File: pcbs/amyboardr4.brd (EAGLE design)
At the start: 111.2 x 50 mm, 123 parts, among them J1 52601-G10-8LF, M13 M2.5, M14 M2.5, M15 M2.5, M16 M2.5, Q2 S8050, Q5 S8050, U1 PCM9211PT, U13 HX3608, U15 H11L1SR2M, U16 SPX3819, U2 ESP32­S2­SOLO, Y1 ABM10W-22.5792MHZ-8-K1Z-T3

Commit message: moving around
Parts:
- Y1: value ABM10W-22.5792MHZ-8-K1Z-T3 -> 22.5792MHZ
- moved L4 101.9 mm to (6.10, 9.14)
- moved C85 79.4 mm to (100.8, 22.6), turned to 90 degrees
- moved SD1 78.8 mm to (91.4, 36.6), turned to 90 degrees
- moved U2 77.6 mm to (13.0, 23.1), turned to 90 degrees
- moved R72 77.4 mm to (94.5, 33.3)
- moved R102 77.4 mm to (100.8, 19.3), turned to 0 degrees
- moved C106 77.2 mm to (95.5, 31.0)
- moved C108 75.0 mm to (100.3, 31.0), turned to 90 degrees
- moved U16 74.8 mm to (100.3, 26.9)
- moved C109 72.8 mm to (89.2, 32.3)
- moved C18 65.8 mm to (4.06, 38.6), turned to 90 degrees
- moved C110 64.3 mm to (86.1, 32.8)
- moved HOST 61.8 mm to (67.1, 36.3), turned to 180 degrees
- moved R88 61.4 mm to (82.3, 32.8), turned to 90 degrees
- moved C88 48.0 mm to (29.0, 14.7)
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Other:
- board size 111.2 x 50 mm -> 107.9 x 50 mm

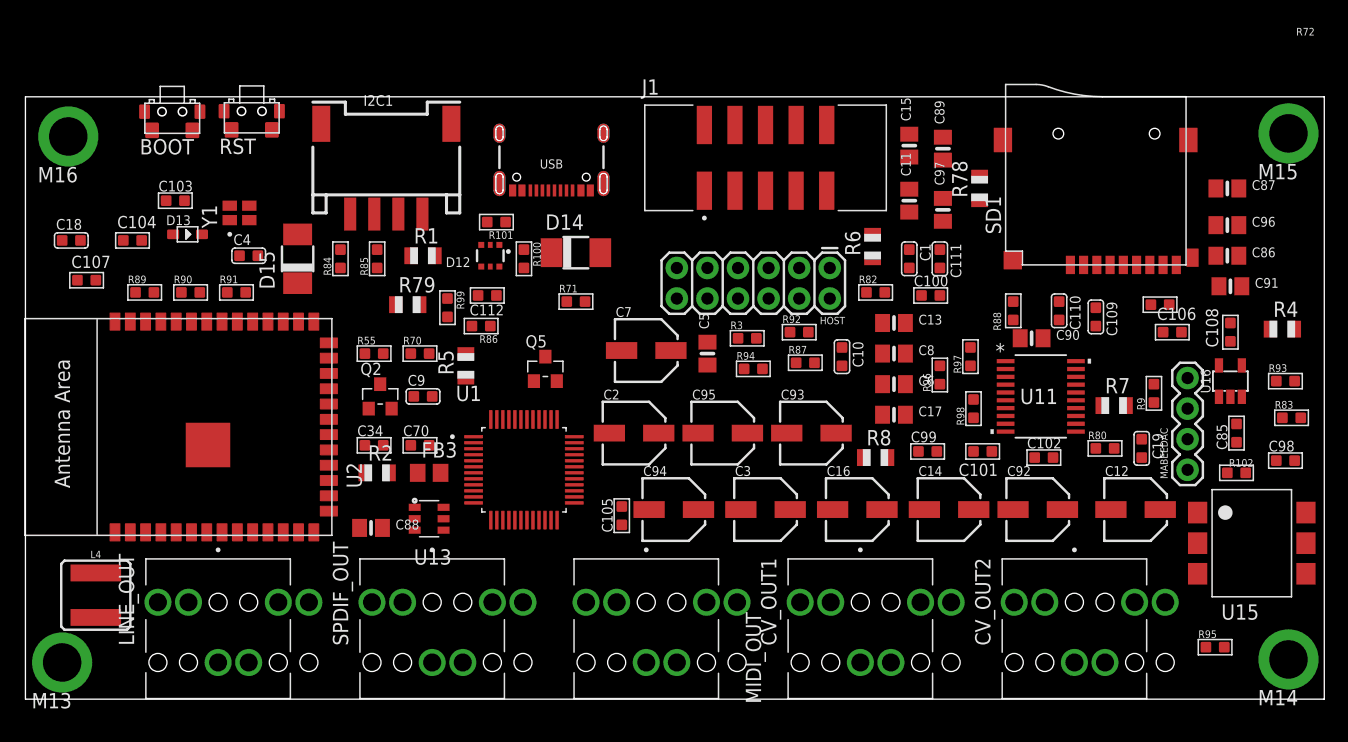
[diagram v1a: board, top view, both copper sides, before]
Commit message: r4 with top jacks
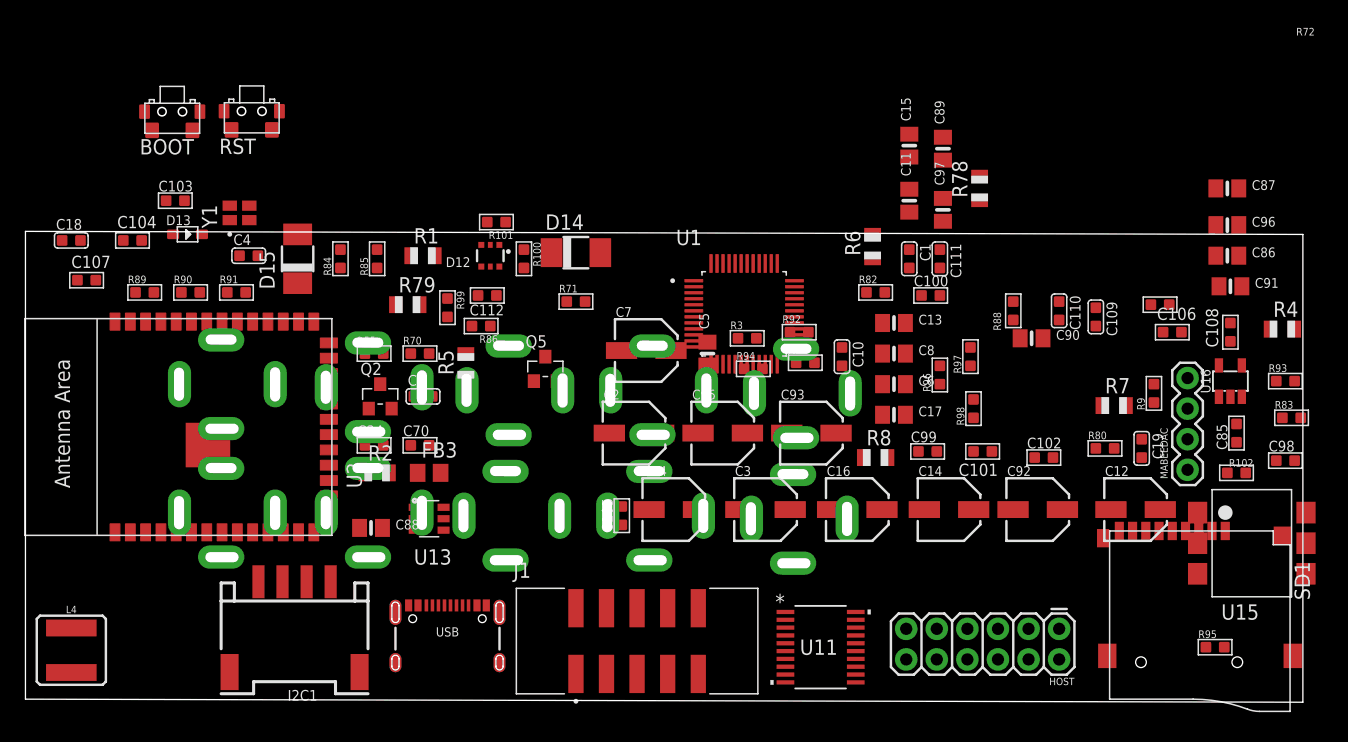
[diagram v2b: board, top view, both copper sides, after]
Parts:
- removed M13, M14, M15, M16: M2.5, sale:M2.5
- removed SPDIF_OUT: SJ1-3543, SJ1-3543:CUI_SJ1-3543
- added U$16: NV-PJ3410_STEREO, PJ3410_sockets:NV-PJ3410_SOCKET
- CV_IN1, CV_IN2, CV_OUT1, CV_OUT2, LINE_IN, LINE_OUT, MIDI_IN, MIDI_OUT, SPDIF_IN: value SJ1-3543 -> NV-PJ3410_STEREO; device SJ1-3543:CUI_SJ1-3543 -> PJ3410_sockets:NV-PJ3410_SOCKET
- moved J1 41.5 mm to (51.1, 5.33)
- moved HOST 35.5 mm to (86.1, 6.35)
- moved USB 34.9 mm to (35.3, 8.64), turned to 0 degrees
- moved CV_IN2 34.0 mm to (64.3, 25.9), turned to 270 degrees
- moved I2C1 31.7 mm to (22.6, 10.2), turned to 180 degrees
- moved CV_IN1 30.1 mm to (52.3, 26.2), turned to 270 degrees
- moved PCM5101 27.7 mm to (66.3, 4.83)
- moved MIDI_IN 26.6 mm to (40.4, 26.2), turned to 270 degrees
- moved CV_OUT2 26.2 mm to (64.0, 15.5), flipped to the bottom, turned to 270 degrees
- moved SPDIF_IN 24.2 mm to (28.7, 26.4), turned to 270 degrees
- moved LINE_IN 23.2 mm to (16.5, 26.7), turned to 270 degrees
- moved SD1 22.5 mm to (95.5, 14.5), turned to 270 degrees
- moved U1 22.4 mm to (59.9, 32.5)
- moved CV_OUT1 21.3 mm to (52.1, 15.7), flipped to the bottom, turned to 270 degrees
- moved MIDI_OUT 16.9 mm to (40.1, 15.7), flipped to the bottom, turned to 270 degrees
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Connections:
- removed net N$15: CV_OUT2.1
- net AGND: now also LINE_IN.GND, LINE_OUT.GND; no longer LINE_IN.1, LINE_OUT.1
- net GND: now also CV_IN1.GND, CV_OUT1.GND, CV_OUT2.GND, MIDI_IN.GND, MIDI_OUT.GND, SPDIF_IN.GND, U$16.GND; no longer CV_IN1.1, CV_IN2.1, CV_OUT1.1, M13.1, M14.1, M15.1, M16.1, MIDI_IN.1, MIDI_OUT.1, SPDIF_IN.1, SPDIF_OUT.1
- net LIN: now also LINE_IN.LEFT/TIP; no longer LINE_IN.2
- net LOUT: now also LINE_OUT.LEFT/TIP; no longer LINE_OUT.2
- net MABEEDAC_VOUT0: now also CV_OUT1.LEFT/TIP; no longer CV_OUT1.2
- net MABEEDAC_VOUT1: now also CV_OUT2.LEFT/TIP; no longer CV_OUT2.2
- net N$10: now also SPDIF_IN.RIGHT/RING; no longer SPDIF_IN.3
- net N$11: now also CV_OUT1.RIGHT/RING; no longer CV_OUT1.3
- net N$12: now also CV_OUT2.RIGHT/RING; no longer CV_OUT2.3
- net N$13: now also CV_IN1.RIGHT/RING; no longer CV_IN1.3
- net N$14: now also CV_IN2.RIGHT/RING; no longer CV_IN2.3
- net N$17: now also CV_IN1.LEFT/TIP; no longer CV_IN1.2
- net N$19: now also CV_IN2.LEFT/TIP; no longer CV_IN2.2
- net N$55: now also MIDI_IN.LEFT/TIP; no longer MIDI_IN.2
- net N$56: now also MIDI_IN.RIGHT/RING; no longer MIDI_IN.3
- net N$58: now also MIDI_OUT.LEFT/TIP; no longer MIDI_OUT.2
- net N$59: now also MIDI_OUT.RIGHT/RING; no longer MIDI_OUT.3
- net N$9: now also U$16.RIGHT/RING; no longer SPDIF_OUT.3
- net RIN: now also LINE_IN.RIGHT/RING; no longer LINE_IN.3
- net ROUT: now also LINE_OUT.RIGHT/RING; no longer LINE_OUT.3
- net SPDIFIN_SIGNAL: now also SPDIF_IN.LEFT/TIP; no longer SPDIF_IN.2
- net SPDIFOUT_SIGNAL: now also U$16.LEFT/TIP; no longer SPDIF_OUT.2
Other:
- board size 107.9 x 50 mm -> 106.1 x 39.1 mm

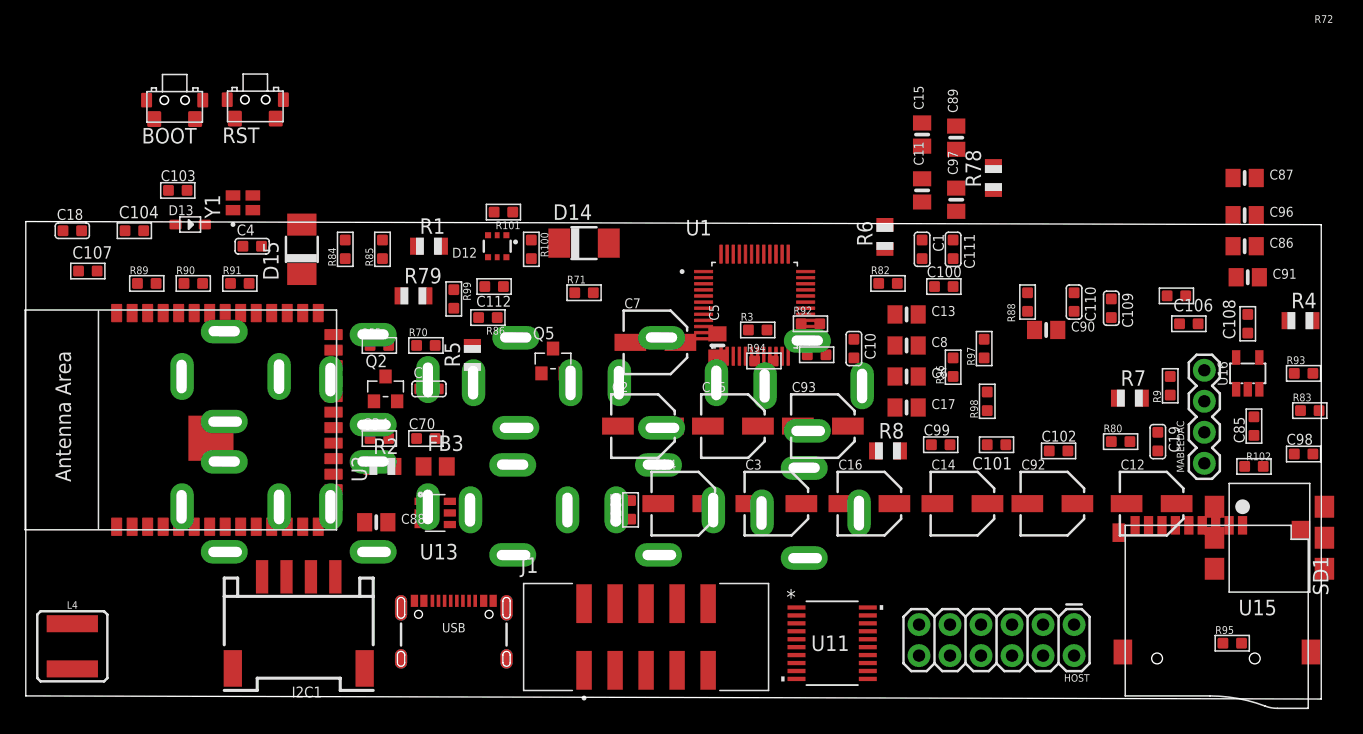
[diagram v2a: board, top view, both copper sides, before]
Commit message: moving jacks together on bottom
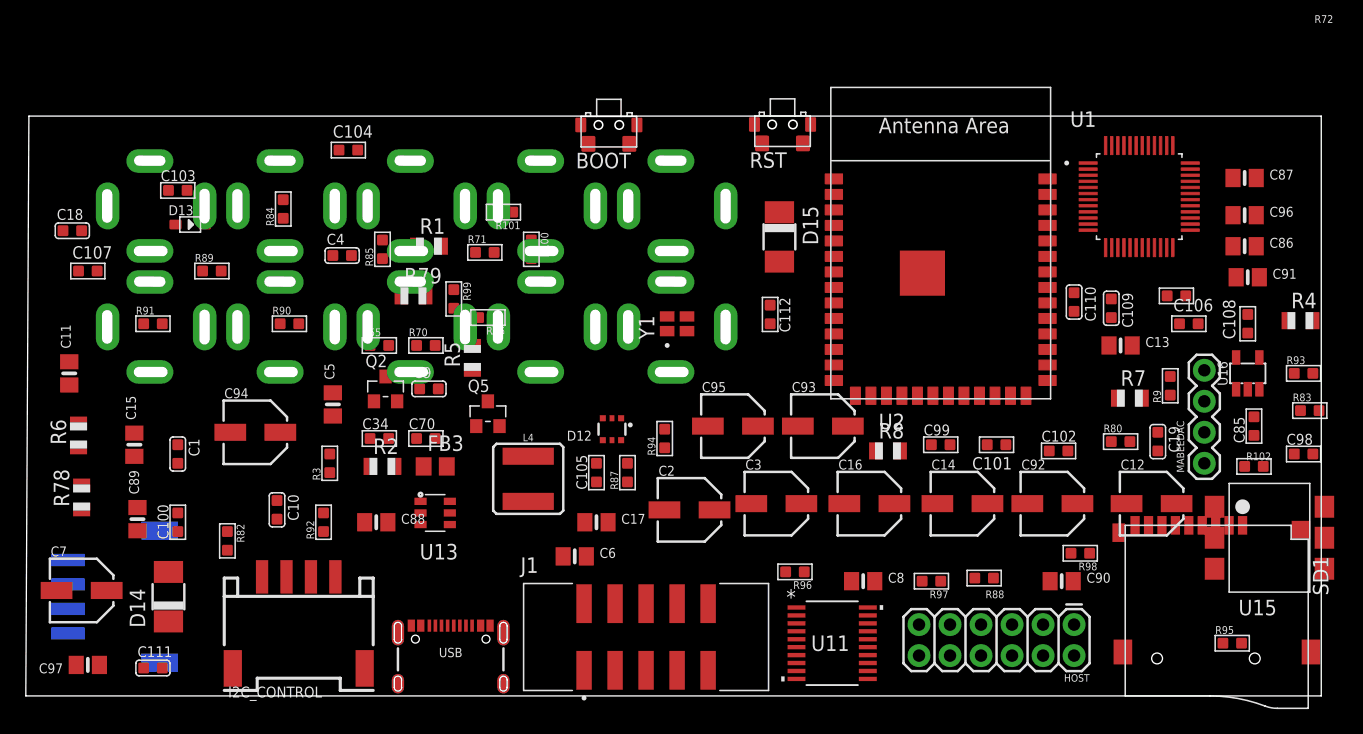
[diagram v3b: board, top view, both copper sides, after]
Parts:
- removed U$16: NV-PJ3410_STEREO, PJ3410_sockets:NV-PJ3410_SOCKET
- added I2C_HOST: (no value), Connector-new:HW4-SMD-2.0-90D
- added SPDIF_OUT: NV-PJ3410_STEREO, PJ3410_sockets:NV-PJ3410_SOCKET
- moved C97 80.7 mm to (5.33, 3.05), turned to 180 degrees
- moved R78 79.1 mm to (4.83, 16.8)
- moved C89 74.0 mm to (9.40, 15.0)
- moved C111 74.0 mm to (10.7, 2.79), turned to 90 degrees
- moved C11 71.4 mm to (3.81, 26.9)
- moved C15 69.3 mm to (9.14, 21.1)
- moved R6 68.0 mm to (4.57, 21.8)
- moved C100 65.6 mm to (12.7, 14.7), turned to 90 degrees
- moved U2 63.9 mm to (75.2, 37.6), turned to 0 degrees
- moved C1 63.2 mm to (12.7, 20.3)
- moved R82 58.1 mm to (16.8, 13.2), turned to 270 degrees
- moved C7 51.2 mm to (4.83, 9.14)
- moved C10 49.1 mm to (20.8, 15.7)
- moved D14 44.7 mm to (11.9, 8.64), turned to 90 degrees
- moved RST 43.2 mm to (62.2, 45.8)
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- renumbered I2C1 to I2C_CONTROL
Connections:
- net +3V3: now also I2C_HOST.3
- net GND: now also I2C_HOST.4, I2C_HOST.SS1, I2C_HOST.SS2, SPDIF_OUT.GND; no longer U$16.GND
- net I2C_SCL: now also I2C_HOST.1
- net I2C_SDA: now also I2C_HOST.2
- net N$9: now also SPDIF_OUT.RIGHT/RING; no longer U$16.RIGHT/RING
- net SPDIFOUT_SIGNAL: now also SPDIF_OUT.LEFT/TIP; no longer U$16.LEFT/TIP
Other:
- board size 106.1 x 39.1 mm -> 106.1 x 47.5 mm

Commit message: adding parts for amyboard
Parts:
- removed MABEEDAC: (no value), SparkFun-Connectors:1X04
- added D1: 1N5819HW-7-F, 1N5819HW-7-F:SOD3715X145N
- added L1: 1269AS-H-100N=P2, 1269AS-H-100N_P2:INDC2520X100N
- added U$7: GP8413, FL5160MX:SOIC-10
- added U3: TPS61040DBVR, TPS61040DBVR:SOT95P280X145-5N
- added U4: TL074CD, TL074CD:SOIC127P600X175-14N
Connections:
- removed net MABEEDAC_VOUT0: CV_OUT1.LEFT/TIP, MABEEDAC.3
- removed net MABEEDAC_VOUT1: CV_OUT2.LEFT/TIP, MABEEDAC.4
- new net CV_OUT0: CV_OUT1.LEFT/TIP
- new net CV_OUT1: CV_OUT2.LEFT/TIP
- new net VCC+: U4.4
- new net VCC-: U4.11
- net +3V3: no longer MABEEDAC.2
- net GND: now also U3.2; no longer MABEEDAC.1

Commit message: Added 8413, TL074, DIP switch, +/-12V rails to schematic.
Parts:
- removed D1: 1N5819HW-7-F, 1N5819HW-7-F:SOD3715X145N
- removed L1: 1269AS-H-100N=P2, 1269AS-H-100N_P2:INDC2520X100N
- removed U3: TPS61040DBVR, TPS61040DBVR:SOT95P280X145-5N
- added C20, C28: 100nF, Discrete-new:C0603
- added C21: 20pF, Discrete-new:C0603
- added C22: 1uF, microbuilder:PANASONIC_C
- added C23, C24, C26, C33: 0.1uF, microbuilder:0805-NO@1
- added C25, C29: 22pF, Discrete-new:C0603
- added C27, C30, C31: 22uF, Discrete-new:C0603
- added C32: 10uF, microbuilder:PANASONIC_C
- added D10, D8, D9: SS54, diode:DO-214AC
- added D4, D5, D6: 1N5819HW-7-F, 1N5819HW-7-F:SOD3715X145N
- added L2: 1269AS-H-100N=P2, 1269AS-H-100N_P2:INDC2520X100N
- added L3: 3.3µH/±30%/3.4A, SparkFun-Coils:CR54
- added R10, R11, R22: 30K, adafruit:R0805
- added R12: 1M, A9G:DISCRETE_R0603
- added R13: 115K, A9G:DISCRETE_R0603
- added R14: 100K, A9G:DISCRETE_R0603
- added R15, R16: NC, A9G:DISCRETE_R0603
- added R17: 0R, A9G:DISCRETE_R0603
- added R18: 228K, A9G:DISCRETE_R0603
- added R19: 12K, A9G:DISCRETE_R0603
- added R20, R23, R24: 10K, adafruit:R0805
- added R21: 15K, adafruit:R0805
- added R25, R26, R29, R30: 22K, adafruit:R0805
- added R27, R28: 51K, adafruit:R0805
- added S1: SWS008, smd-special:SMS-008
- added U5: TPS61040DBVR, TPS61040DBVR:SOT95P280X145-5N
- added U6: HX3608, self:SOT-23-6
- R1, R2: value 10K -> 51K
- R5: value 68K -> 10K
- R6: value 33K -> 15K
- R7: value 68K -> 30K
- R8: value 33K -> 30K
- moved C3 1330.5 mm to (-363.2, -1244.6)
- moved C2 1325.6 mm to (-356.1, -1244.6)
- moved R8 1252.1 mm to (-343.4, -1161.0)
- moved R5 387.3 mm to (-343.4, 101.6), turned to 0 degrees
- moved C10 371.3 mm to (-339.3, 105.9)
- moved R6 358.4 mm to (-343.4, 107.4), turned to 0 degrees
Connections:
- removed net CV_OUT0: CV_OUT1.LEFT/TIP
- removed net VCC+: U4.4
- removed net VCC-: U4.11
- new net 12V: C27.1, C28.1, C29.1, D8.C, R17.2, R18.2
- new net ADC2: C9.1, R7.2, S1.10
- new net CV_OUT2: CV_OUT2.LEFT/TIP, R10.2, R11.2, U4.7
- new net LOUT_2V: C97.1, R79.1, U4.10
- new net N$15: R20.2, R21.1, S1.7
- new net N$16: R5.2, R6.1, S1.8
- new net N$18: C24.1, U$7.8, U4.3
- new net N$20: C23.1, U$7.7, U4.5
- new net N$21: C30.1, D8.A, L3.P$2, U6.1
- new net N$22: C22.+, U$7.10
- new net N$23: D4.A, L2.1, U5.1
- new net N$24: C25.1, D4.C, R12.2
- new net N$25: C25.2, R12.1, R13.2, U5.3
- new net N$26: C29.2, R18.1, R19.2, U6.3
- new net N$27: R15.2, U6.6
- new net N$28: R16.1, R17.1, U6.5
- new net N$29: C30.2, D10.C, D9.A
- new net N$30: R23.1, S1.6
- new net N$31: R10.1, R11.1, S1.12, U4.6
- new net N$32: R24.1, S1.5
- new net N$33: R22.1, S1.11, U4.2
- new net N$35: R26.1, S1.1
- new net N$36: R25.1, S1.2
- new net N$40: R29.1, S1.4
- new net N$41: R30.1, S1.3
- new net N$44: R27.1, S1.15, U4.9
- new net N$45: R28.1, S1.16, U4.13
- new net ROUT_2V: C96.1, R78.1, U4.12
- net +12V: now also C21.1, C26.1, U$7.5, U4.4
- net +3V3: now also C32.+, C33.1, L2.2, R20.1, R23.2, R24.2, R5.1, U5.4, U5.5
- net -12V: now also C20.2, C21.2, C31.2, D10.A, U4.11
- net ADC0: no longer C10.1, R5.2, R6.1
- net ADC1: now also C10.1, R8.2, S1.9; no longer C9.1, R7.2, R8.1
- net AGND: now also C32.-, C33.2, R25.2, R26.2, R29.2, R30.2
- net CV_OUT1: now also CV_OUT1.LEFT/TIP, R22.2, U4.1; no longer CV_OUT2.LEFT/TIP
- net ENABLE: now also R14.1, U6.4
- net GND: now also C20.1, C22.-, C23.2, C24.2, C26.2, C27.2, C28.2, C31.1, D9.C, R13.1, R15.1, R19.1, R21.2, U$7.3, U$7.4, U$7.6, U$7.9, U5.2, U6.2; no longer R8.2, U3.2
- net I2C_SCL: now also U$7.1
- net I2C_SDA: now also U$7.2
- net LIN: now also R2.2; no longer C2.-
- net LINX: now also C2.+; no longer R2.2
- net LOUT: now also R27.2, U4.8; no longer C97.1, R79.1
- net N$17: now also R8.1; no longer R5.1
- net N$4: now also C2.-, S1.13; no longer C2.+
- net N$5: now also C3.-, R1.1, S1.14; no longer C3.+, R1.2
- net RIN: now also R1.2; no longer C3.-
- net RINX: now also C3.+; no longer R1.1
- net ROUT: now also R28.2, U4.14; no longer C96.1, R78.1
- net VPWR: now also L3.P$1, R14.2, R16.2

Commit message: removing other boost
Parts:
- removed C25: 22pF, Discrete-new:C0603
- removed D4, D5, D6: 1N5819HW-7-F, 1N5819HW-7-F:SOD3715X145N
- removed L2: 1269AS-H-100N=P2, 1269AS-H-100N_P2:INDC2520X100N
- removed R12: 1M, A9G:DISCRETE_R0603
- removed R13: 115K, A9G:DISCRETE_R0603
- removed U5: TPS61040DBVR, TPS61040DBVR:SOT95P280X145-5N
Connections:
- removed net N$23: D4.A, L2.1, U5.1
- removed net N$24: C25.1, D4.C, R12.2
- removed net N$25: C25.2, R12.1, R13.2, U5.3
- net +3V3: no longer L2.2, U5.4, U5.5
- net GND: no longer R13.1, U5.2

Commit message: 4 way DIN, VPWR
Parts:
- removed C101, C104: 10uF, Discrete:0603
- removed C102: 0.1uF, A9G:DISCRETE_C0603
- removed C105: 10uF, A9G:DISCRETE_C0603
- removed C109: 22uF, Discrete-new:C0603
- removed C110: 100nF, Discrete-new:C0603
- removed C111: 22pF, Discrete-new:C0603
- removed D15: SS54, diode:DO-214AC
- removed L4: 3.3µH/±30%/3.4A, SparkFun-Coils:CR54
- removed R23, R24: 10K, adafruit:R0805
- removed R92: 0R, Discrete:R0603
- removed R93: 100K, A9G:DISCRETE_R0603
- removed R94, R95: NC, A9G:DISCRETE_R0603
- removed R96: 0R, A9G:DISCRETE_R0603
- removed R97: 88.7K, A9G:DISCRETE_R0603
- removed R98: 12K, A9G:DISCRETE_R0603
- removed S1: SWS008, smd-special:SMS-008
- removed U13: HX3608, self:SOT-23-6
- added 1-10VPP: 218-4LPSTR, 218-4LPSTR:SW_218-4LPSTR
- added C35: NC, Discrete:0603
- added D1, D2: SS54, diode:DO-214AC
- added U3: SPX3819, IC:SOT23-5
- C32: value 10uF -> 4.7uF/16V; device microbuilder:PANASONIC_C -> Discrete:0603
- C33: value 0.1uF -> 10uF; device microbuilder:0805-NO@1 -> Discrete:0603
- moved R26 1320.6 mm to (39.9, 38.9)
- moved R28 1320.6 mm to (39.9, 27.2)
- moved C2 1320.6 mm to (34.0, 17.0)
- moved C3 1320.6 mm to (26.9, 17.0)
- moved R25 1320.6 mm to (39.9, 44.7)
- moved R27 1320.6 mm to (39.9, 33.0)
- moved R29 1320.6 mm to (39.9, 21.3)
- moved R30 1320.6 mm to (39.9, 15.5)
- moved C26 1242.6 mm to (4.57, 20.6)
- moved R10 1242.6 mm to (5.08, 16.3)
- moved R8 1242.6 mm to (11.9, 29.7)
- moved C22 1242.6 mm to (6.35, 31.2)
- moved C23 1242.6 mm to (4.57, 25.7)
- moved C24 1242.6 mm to (4.57, 23.1)
- moved R11 1242.6 mm to (5.08, 10.4)
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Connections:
- net VBUS renamed 5V_IN
- removed net N$16: R5.2, R6.1, S1.8
- removed net N$30: R23.1, S1.6
- removed net N$32: R24.1, S1.5
- removed net N$65: D15.A, L4.P$2, U13.1
- removed net N$66: C111.2, R97.1, R98.2, U13.3
- removed net N$67: R94.2, U13.6
- removed net N$68: R95.1, R96.1, U13.5
- new net 12V_IN: D2.A, J1.09, J1.10
- new net 3V3_IN: D1.A, I2C_CONTROL.3
- net +12V: no longer J1.09, J1.10
- net +3V3: no longer C105.2, C32.+, C33.1, I2C_CONTROL.3, R23.2, R24.2, R92.1
- net -12V: no longer J1.01, J1.02
- net 3.3V: no longer C104.1, R92.2
- net 5V: now also C33.1, U3.5; no longer C101.1, C102.2, C109.1, C110.1, C111.1, D14.C, D15.C, R96.2, R97.2
- net ADC1: now also R5.2, R6.1; no longer S1.9
- net ADC2: now also R20.2, R21.1; no longer S1.10
- net AGND: no longer C32.-, C33.2
- net ENABLE: no longer R93.1, U13.4
- net GND: now also C32.2, C33.2, C35.2, J1.01, J1.02, U3.2; no longer C101.2, C102.1, C104.2, C105.1, C109.2, C110.2, R94.1, R98.1, U13.2
- net N$15: now also C35.1, U3.4; no longer R20.2, R21.1, S1.7
- net N$31: no longer S1.12
- net N$33: no longer S1.11
- net N$35: now also 1-10VPP.5; no longer S1.1
- net N$36: now also 1-10VPP.6; no longer S1.2
- net N$4: now also 1-10VPP.1; no longer S1.13
- net N$40: now also 1-10VPP.8; no longer S1.4
- net N$41: now also 1-10VPP.7; no longer S1.3
- net N$44: now also 1-10VPP.3; no longer S1.15
- net N$45: now also 1-10VPP.4; no longer S1.16
- net N$5: now also 1-10VPP.2; no longer S1.14
- net VPWR: now also C32.1, D1.C, D14.C, D2.C, U3.1, U3.3; no longer L4.P$1, R93.2, R95.2
